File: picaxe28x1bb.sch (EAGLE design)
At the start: 40 parts, among them Q1 16MHz, U1 PICAXE-28X2, U2 74AHC1G04, U3 74AHC1G04, X1 VIN, X2 GND

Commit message: updated layout, leds, inverted serial, etc.
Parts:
- removed R11, R12: 330, resistor:R-US_R0603
- added R6, R8: 330, resistor:R-US_R0603
- LED1, LED2, LED3, PWR: device bt_opto:LEDCHIPLED_0603 -> bt_opto:LEDCHIPLED_0805
- S2: value OFF ON -> SPDT_OS102011MAQN1
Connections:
- net C.1: no longer R4.2
- net C.7: now also R8.1
- net N$1: now also R8.2; no longer R4.1
- net N$2: now also R6.2; no longer R5.1
- net N$5: now also R4.2; no longer R11.1
- net N$7: now also R5.2; no longer R12.1
- net RXD: now also R5.1; no longer R12.2
- net TXD: now also R4.1; no longer R11.2
- net VDD: now also R6.1; no longer R5.2
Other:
- moved on the sheet: R4, R5
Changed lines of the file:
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@@
 <part name="U$9" library="bt" deviceset="VDD" device="" value="5V"/>
 <part name="GND5" library="bt" deviceset="GND" device=""/>
-<part name="S2" library="bt_electromech" deviceset="SPDT" device="_OS102011MAQN1" value="OFF     ON"/>
+<part name="S2" library="bt_electromech" deviceset="SPDT" device="_OS102011MAQN1" value=""/>
 <part name="U$10" library="bt" deviceset="BTLOGO" device="-LOGO-MD"/>
 <part name="U1" library="bt_pic" deviceset="PICAXE-28X2" device=""/>
@@
 <part name="C1" library="rcl" deviceset="C-US" device="C0603" value="104"/>
 <part name="GND8" library="bt" deviceset="GND" device=""/>
-<part name="PWR" library="bt_opto" deviceset="LED" device="CHIPLED_0603"/>
-<part name="LED2" library="bt_opto" deviceset="LED" device="CHIPLED_0603" value="C.1"/>
-<part name="R4" library="resistor" deviceset="R-US_" device="R0603" value="330"/>
+<part name="PWR" library="bt_opto" deviceset="LED" device="CHIPLED_0805"/>
+<part name="LED2" library="bt_opto" deviceset="LED" device="CHIPLED_0805" value="C.1"/>
 <part name="GND9" library="bt" deviceset="GND" device=""/>
-<part name="R5" library="resistor" deviceset="R-US_" device="R0603" value="330"/>
 <part name="R7" library="resistor" deviceset="R-US_" device="R0603" value="10K"/>
 <part name="GND10" library="bt" deviceset="GND" device=""/>
@@
 <part name="GND11" library="bt" deviceset="GND" device=""/>
 <part name="D1" library="bt_diode" deviceset="DIODE" device="_SOD123FL" value="DIODE"/>
-<part name="LED1" library="bt_opto" deviceset="LED" device="CHIPLED_0603" value="TX"/>
-<part name="R11" library="resistor" deviceset="R-US_" device="R0603" value="330"/>
-<part name="LED3" library="bt_opto" deviceset="LED" device="CHIPLED_0603" value="RX"/>
+<part name="LED1" library="bt_opto" deviceset="LED" device="CHIPLED_0805" value="TX"/>
+<part name="LED3" library="bt_opto" deviceset="LED" device="CHIPLED_0805" value="RX"/>
 <part name="GND15" library="bt" deviceset="GND" device=""/>
 <part name="GND16" library="bt" deviceset="GND" device=""/>
 <part name="U$12" library="bt" deviceset="VDD" device="" value="5V"/>
-<part name="R12" library="resistor" deviceset="R-US_" device="R0603" value="330"/>
 <part name="C2" library="rcl" deviceset="C-US" device="C0603" value="104"/>
 <part name="U2" library="74xx-little-us" deviceset="74*1G04" device="DBV" technology="AHC" value="74AHC1G04"/>
@@
 <part name="U$14" library="bt" deviceset="VDD" device="" value="5V"/>
 <part name="GND13" library="bt" deviceset="GND" device=""/>
+<part name="R4" library="resistor" deviceset="R-US_" device="R0603" value="330"/>
+<part name="R5" library="resistor" deviceset="R-US_" device="R0603" value="330"/>
+<part name="R6" library="resistor" deviceset="R-US_" device="R0603" value="330"/>
+<part name="R8" library="resistor" deviceset="R-US_" device="R0603" value="330"/>
 </parts>
 <sheets>
@@
 <instance part="PWR" gate="G$1" x="180.34" y="121.92"/>
 <instance part="LED2" gate="G$1" x="195.58" y="121.92" rot="MR0"/>
-<instance part="R4" gate="G$1" x="195.58" y="132.08" rot="R90"/>
 <instance part="GND9" gate="1" x="195.58" y="111.76"/>
-<instance part="R5" gate="G$1" x="180.34" y="132.08" rot="R90"/>
 <instance part="R7" gate="G$1" x="119.38" y="45.72" rot="R270"/>
 <instance part="GND10" gate="1" x="119.38" y="35.56"/>
@@
 <instance part="D1" gate="D1" x="152.4" y="139.7" rot="R90"/>
 <instance part="LED1" gate="G$1" x="76.2" y="104.14"/>
-<instance part="R11" gate="G$1" x="76.2" y="114.3" rot="R90"/>
 <instance part="LED3" gate="G$1" x="104.14" y="104.14"/>
 <instance part="GND15" gate="1" x="104.14" y="93.98"/>
 <instance part="GND16" gate="1" x="180.34" y="111.76"/>
 <instance part="U$12" gate="G$1" x="180.34" y="144.78"/>
-<instance part="R12" gate="G$1" x="104.14" y="114.3" rot="R90"/>
 <instance part="C2" gate="G$1" x="297.18" y="129.54"/>
 <instance part="U2" gate="A" x="91.44" y="132.08"/>
@@
 <instance part="U$14" gate="G$1" x="134.62" y="149.86"/>
 <instance part="GND13" gate="1" x="76.2" y="93.98"/>
+<instance part="R4" gate="G$1" x="76.2" y="114.3" rot="R270"/>
+<instance part="R5" gate="G$1" x="104.14" y="114.3" rot="R270"/>
+<instance part="R6" gate="G$1" x="180.34" y="132.08" rot="R270"/>
+<instance part="R8" gate="G$1" x="195.58" y="132.08" rot="R270"/>
 </instances>
 <busses>
@@
 <pinref part="JP7" gate="A" pin="8"/>
 <pinref part="U1" gate="U1" pin="C.7~|KDA|HRX"/>
+</segment>
+<segment>
+<wire x1="195.58" y1="137.16" x2="195.58" y2="139.7" width="0.1524" layer="91"/>
+<wire x1="195.58" y1="139.7" x2="190.5" y2="139.7" width="0.1524" layer="91"/>
+<label x="190.5" y="139.7" size="1.778" layer="95"/>
+<pinref part="R8" gate="G$1" pin="1"/>
 </segment>
 </net>
@@
 </segment>
 <segment>
-<pinref part="R5" gate="G$1" pin="2"/>
 <pinref part="U$12" gate="G$1" pin="VDD"/>
 <wire x1="180.34" y1="142.24" x2="180.34" y2="137.16" width="0.1524" layer="91"/>
+<pinref part="R6" gate="G$1" pin="1"/>
 </segment>
 <segment>
@@
 <wire x1="43.18" y1="132.08" x2="76.2" y2="132.08" width="0.1524" layer="91"/>
 <pinref part="U2" gate="A" pin="I"/>
-<pinref part="R11" gate="G$1" pin="2"/>
 <wire x1="76.2" y1="132.08" x2="81.28" y2="132.08" width="0.1524" layer="91"/>
 <wire x1="76.2" y1="119.38" x2="76.2" y2="132.08" width="0.1524" layer="91"/>
 <junction x="76.2" y="132.08"/>
+<pinref part="R4" gate="G$1" pin="1"/>
 </segment>
 </net>
@@
 <pinref part="U3" gate="A" pin="O"/>
 <wire x1="124.46" y1="121.92" x2="119.38" y2="121.92" width="0.1524" layer="91"/>
-<pinref part="R12" gate="G$1" pin="2"/>
 <wire x1="119.38" y1="121.92" x2="104.14" y2="121.92" width="0.1524" layer="91"/>
 <wire x1="104.14" y1="121.92" x2="104.14" y2="119.38" width="0.1524" layer="91"/>
 <junction x="119.38" y="121.92"/>
+<pinref part="R5" gate="G$1" pin="1"/>
 </segment>
 </net>
@@
 <wire x1="45.72" y1="55.88" x2="33.02" y2="55.88" width="0.1524" layer="91"/>
 </segment>
-<segment>
-<pinref part="R4" gate="G$1" pin="2"/>
-<wire x1="195.58" y1="137.16" x2="195.58" y2="139.7" width="0.1524" layer="91"/>
-<wire x1="195.58" y1="139.7" x2="190.5" y2="139.7" width="0.1524" layer="91"/>
-<label x="190.5" y="139.7" size="1.778" layer="95"/>
-</segment>
 </net>
 <net name="C.2" class="0">
@@
 <segment>
 <pinref part="LED2" gate="G$1" pin="A"/>
-<pinref part="R4" gate="G$1" pin="1"/>
 <wire x1="195.58" y1="127" x2="195.58" y2="124.46" width="0.1524" layer="91"/>
+<pinref part="R8" gate="G$1" pin="2"/>
 </segment>
 </net>
 <net name="N$2" class="0">
 <segment>
-<pinref part="R5" gate="G$1" pin="1"/>
 <pinref part="PWR" gate="G$1" pin="A"/>
 <wire x1="180.34" y1="124.46" x2="180.34" y2="127" width="0.1524" layer="91"/>
+<pinref part="R6" gate="G$1" pin="2"/>
 </segment>
 </net>
@@
 <segment>
 <pinref part="LED1" gate="G$1" pin="A"/>
-<pinref part="R11" gate="G$1" pin="1"/>
 <wire x1="76.2" y1="109.22" x2="76.2" y2="106.68" width="0.1524" layer="91"/>
+<pinref part="R4" gate="G$1" pin="2"/>
 </segment>
 </net>
@@
 <segment>
 <pinref part="LED3" gate="G$1" pin="A"/>
-<pinref part="R12" gate="G$1" pin="1"/>
 <wire x1="104.14" y1="109.22" x2="104.14" y2="106.68" width="0.1524" layer="91"/>
-</segment>
-</net>
+<pinref part="R5" gate="G$1" pin="2"/>
+</segment>
+</net>

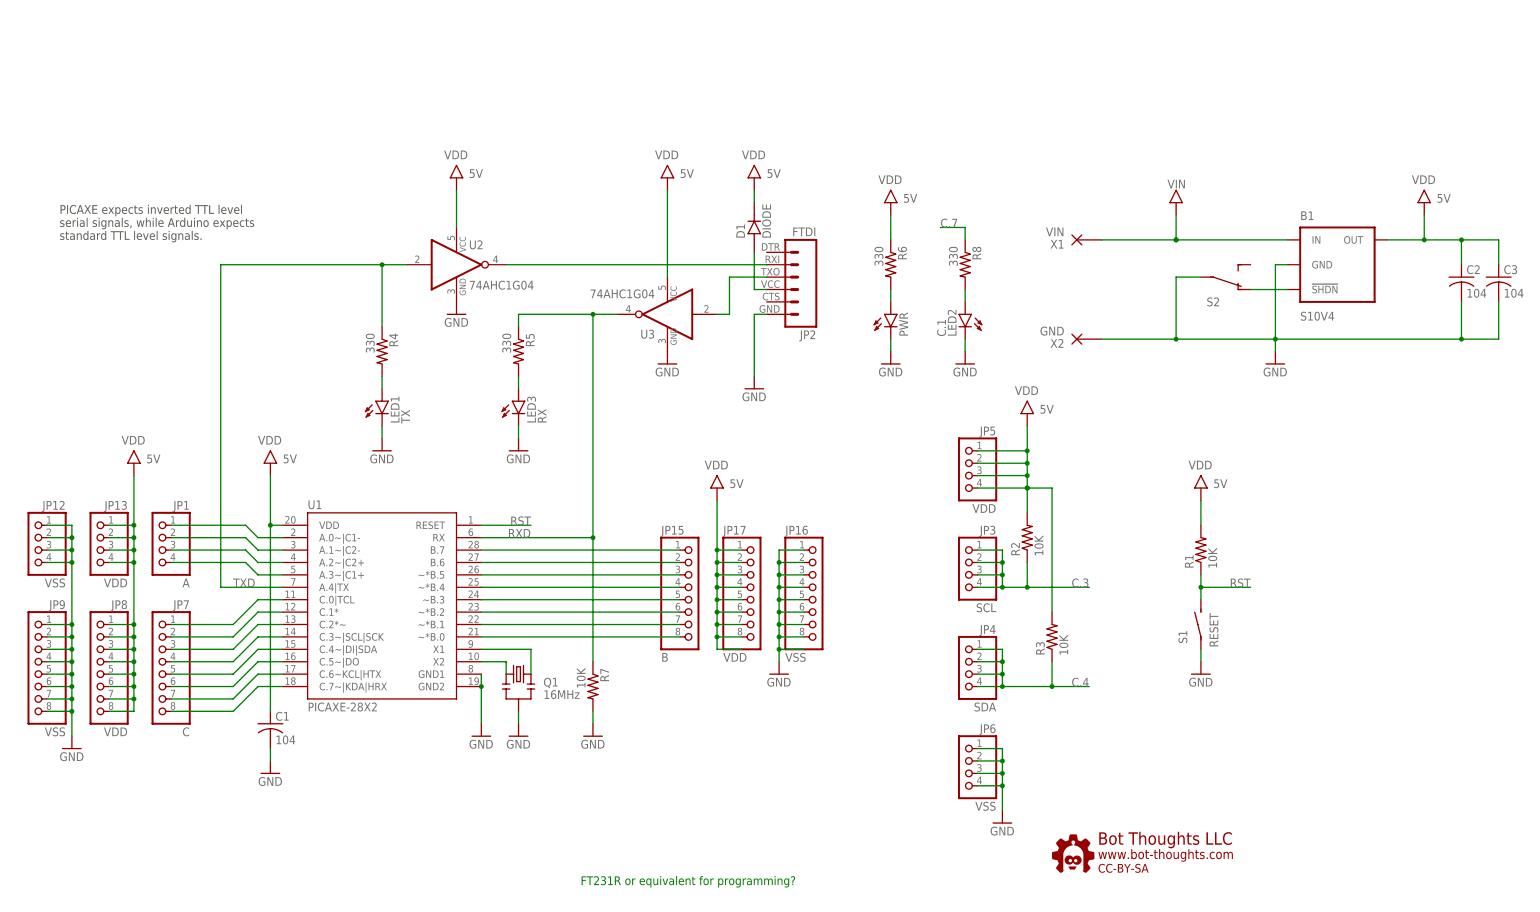
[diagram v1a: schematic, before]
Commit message: addition of FTDI, usb mini b, layout updates
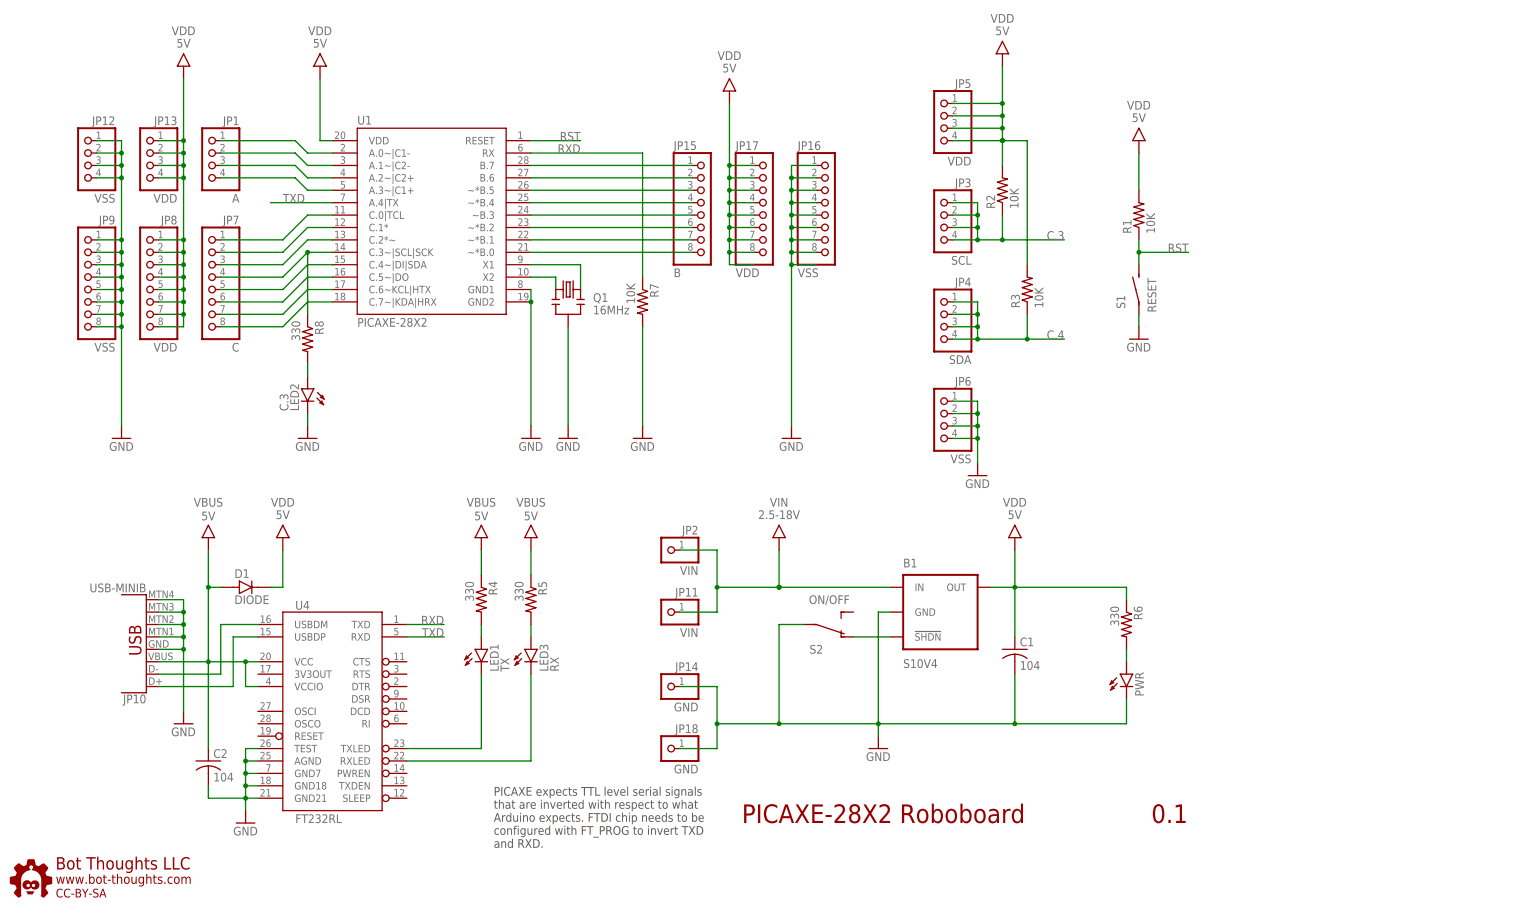
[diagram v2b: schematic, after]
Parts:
- removed C3: 104, rcl:C-USC0603
- removed U2, U3: 74AHC1G04, 74xx-little-us:74AHC1G04DBV
- removed X1: VIN, bt_electromech:WIREPAD_18GA
- removed X2: GND, bt_electromech:WIREPAD_18GA
- added JP10: USB-MINIB, bt_electromech:USB-MINIB
- added JP11: VIN, pinhead-2:PINHD-1X01_2.54-S
- added JP14, JP18: GND, pinhead-2:PINHD-1X01_2.54-S
- added U4: FT232RL, SparkFun-DigitalIC:FT232RLSSOP
- JP2: value FTDI -> VIN; device SparkFun-Connectors:FTDI_BASICPTH -> pinhead-2:PINHD-1X01_2.54-S
- LED2: value C.1 -> C.3; device bt_opto:LEDCHIPLED_0805 -> bt_opto:LEDCHIPLED_1206
- PWR: device bt_opto:LEDCHIPLED_0805 -> bt_opto:LEDCHIPLED_1206
- S2: value SPDT_OS102011MAQN1 -> ON/OFF
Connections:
- removed net RXI: JP2.2, U2A.O
- removed net TXO: JP2.3, U3A.I
- new net N$10: LED3.C, U4.RXLED
- new net N$8: JP10.D-, U4.USBDM
- new net N$9: JP10.D+, U4.USBDP
- new net VBUS: C2.1, D1.A, JP10.VBUS, R4.1, R5.1, U4.VCC, U4.VCCIO
- net C.3: now also R8.1
- net C.7: no longer R8.1
- net GND: now also JP10.GND, JP10.SHIELD1, JP10.SHIELD2, JP10.SHIELD3, JP10.SHIELD4, JP14.1, JP18.1, U4.AGND, U4.GND18, U4.GND21, U4.GND7, U4.TEST; no longer C3.2, JP2.6, LED1.C, LED3.C, U2P.GND, U3P.GND, X2.P
- net N$3: now also LED1.C, U4.TXLED; no longer D1.A, JP2.4
- net RXD: now also U4.TXD; no longer R5.1, U3A.O
- net TXD: now also U4.RXD; no longer R4.1, U2A.I
- net VDD: no longer C2.1, C3.1, U2P.VCC, U3P.VCC
- net VIN: now also JP11.1, JP2.1; no longer X1.P
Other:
- note added: "0.1"
- note added: "PICAXE expects TTL level serial signals that are inverted with respect to what Arduino expects. FTDI chip needs to be configured with FT_PROG to invert TXD and RXD."
- note added: "PICAXE-28X2 Roboboard"
- note removed: "FT231R or equivalent for programming?"
- note removed: "PICAXE expects inverted TTL level serial signals, while Arduino expects standard TTL level signals."
- moved on the sheet: B1, C1, C2, D1, JP1, JP12, JP13, JP15, JP16, JP17, JP3, JP4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
